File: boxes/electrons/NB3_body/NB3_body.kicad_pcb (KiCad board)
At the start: 2 copper layers, 200 x 199.5 mm, 45 parts, among them J1 Conn_02x05_Counter_Clockwise, J10 JST SH 4-way Socket, J12 Conn_02x03_Top_Bottom, J13 Conn_02x03_Top_Bottom, J14 Conn_02x05_Counter_Clockwise, J15 Conn_02x05_Counter_Clockwise, J2 Conn_02x05_Counter_Clockwise, J3 Conn_02x05_Counter_Clockwise, J4 Conn_02x05_Counter_Clockwise, J5 Conn_02x05_Counter_Clockwise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

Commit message: Work on PCBs (v1 and v2)
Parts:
- added H31: MountingHole, MountingHole:MountingHole_2.7mm_M2.5_ISO7380_Pad, F.Cu at (94.0, 161.0)
- added H32: MountingHole, MountingHole:MountingHole_2.7mm_M2.5_ISO7380_Pad, F.Cu at (155.0, 161.0)
- added J11: JST SH 4-way Socket, NB3_body:Connector_S4B-PH-SM4-TB(LF)(SN), F.Cu at (124.5, 78.0)
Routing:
- net /WS: track 320.0 -> 163.1 mm, vias 10 -> 6
- net /SDI: track 251.1 -> 99.5 mm, vias 6 -> 3
- net +3V3: track 271.5 -> 132.1 mm, vias 8 -> 5
- net /SCK: track 290.6 -> 157.4 mm, vias 4 -> 3
- net /LE: track 246.1 -> 172.1 mm
- net /LF: track 240.9 -> 170.1 mm
- net /LG: track 235.7 -> 168.2 mm
- net /LD: track 226.0 -> 159.0 mm
- net /LH: track 230.6 -> 166.4 mm
- net GND: track 128.0 -> 136.8 mm, vias 36 -> 42
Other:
- outline, holes or cut-outs redrawn
- board text added: "NB3_body Rev 0.0.6 For Research and Education ONLY"
- board text removed: "NB3_body Rev 0.0.5 For Research and Education ONLY"

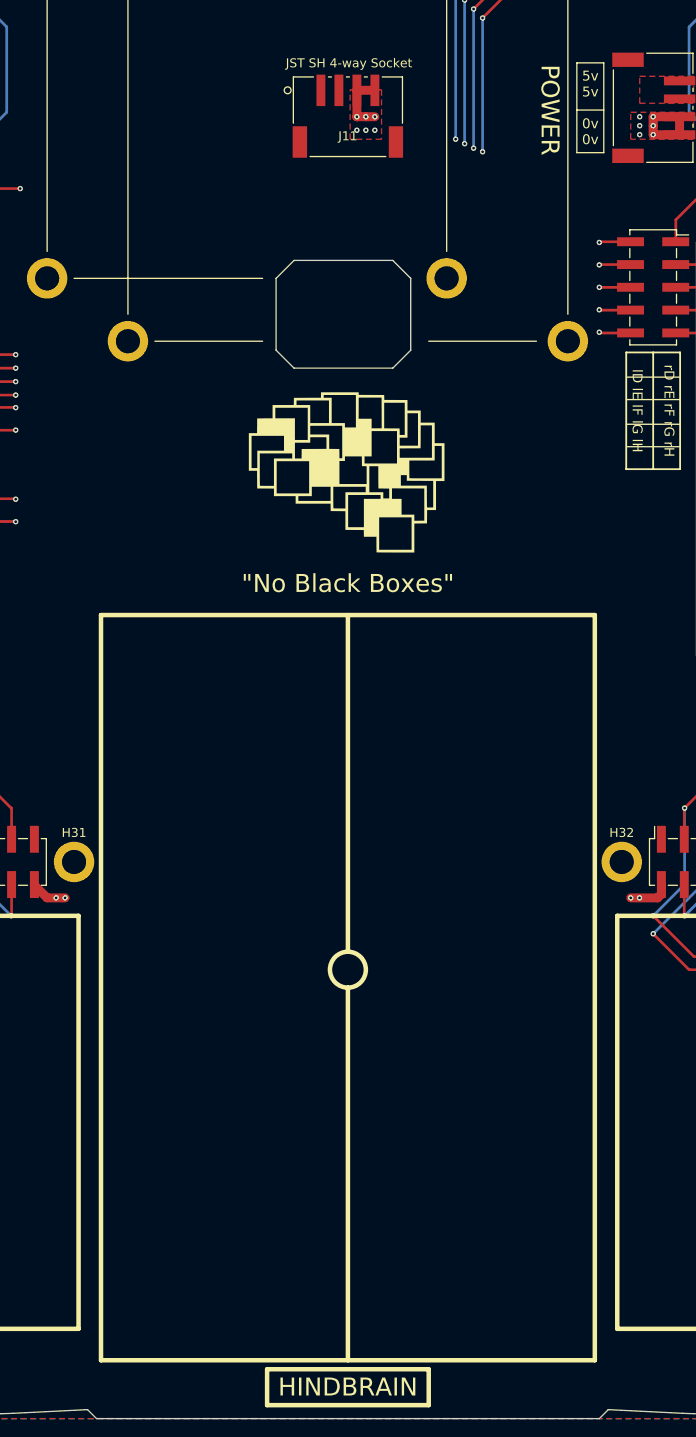
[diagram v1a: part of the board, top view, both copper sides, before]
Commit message: PCB tweaks (charger and body)
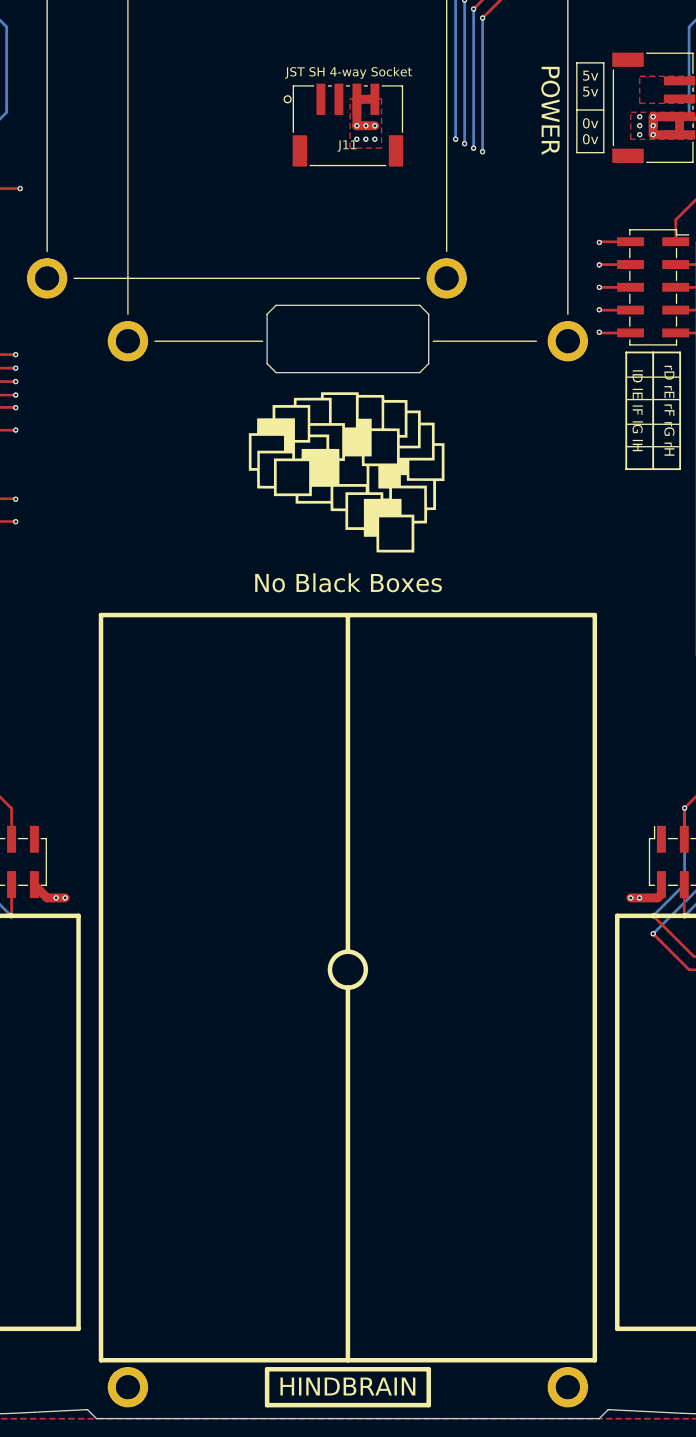
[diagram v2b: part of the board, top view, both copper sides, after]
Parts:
- moved H31 58.8 mm to (100.0, 219.5)
- moved H32 58.8 mm to (149.0, 219.5)
- moved J11 1.00 mm to (124.5, 79.0)
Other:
- outline, holes or cut-outs redrawn
- board text added: "No Black Boxes"
- board text removed: "{dblquote}No Black Boxes{dblquote}"

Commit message: Update NB3 Body (rev 6)
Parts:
- added G***: LOGO, NB3_body:Logo_VK_15mm, B.Cu at (124.5, 196.0)
- J12, J13: footprint Connector_PinHeader_2.54mm:PinHeader_2x03_P2.54mm_Vertical_SMD -> Connector_PinHeader_2.54mm:PinHeader_2x03_P2.54mm_Vertical
- moved J13 2.85 mm to (200.2, 166.5)
- moved J12 2.83 mm to (46.2, 166.5)
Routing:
- net /SCK: track 157.4 -> 326.8 mm, vias 3 -> 7
- net /WS: track 163.1 -> 323.8 mm, vias 6 -> 8
- net /SDI: track 99.5 -> 259.9 mm, vias 3 -> 7
- net +3V3: track 132.1 -> 285.2 mm, vias 5 -> 7
- net /LG: track 168.2 -> 249.9 mm
- net /LF: track 170.1 -> 251.5 mm
- net /LE: track 172.1 -> 252.8 mm
- net /LH: track 166.4 -> 245.1 mm
- net /LD: track 159.0 -> 237.6 mm
- net /LB: track 183.9 -> 188.1 mm
- net /LA: track 190.6 -> 189.2 mm
- net /RA: track 201.3 -> 202.5 mm

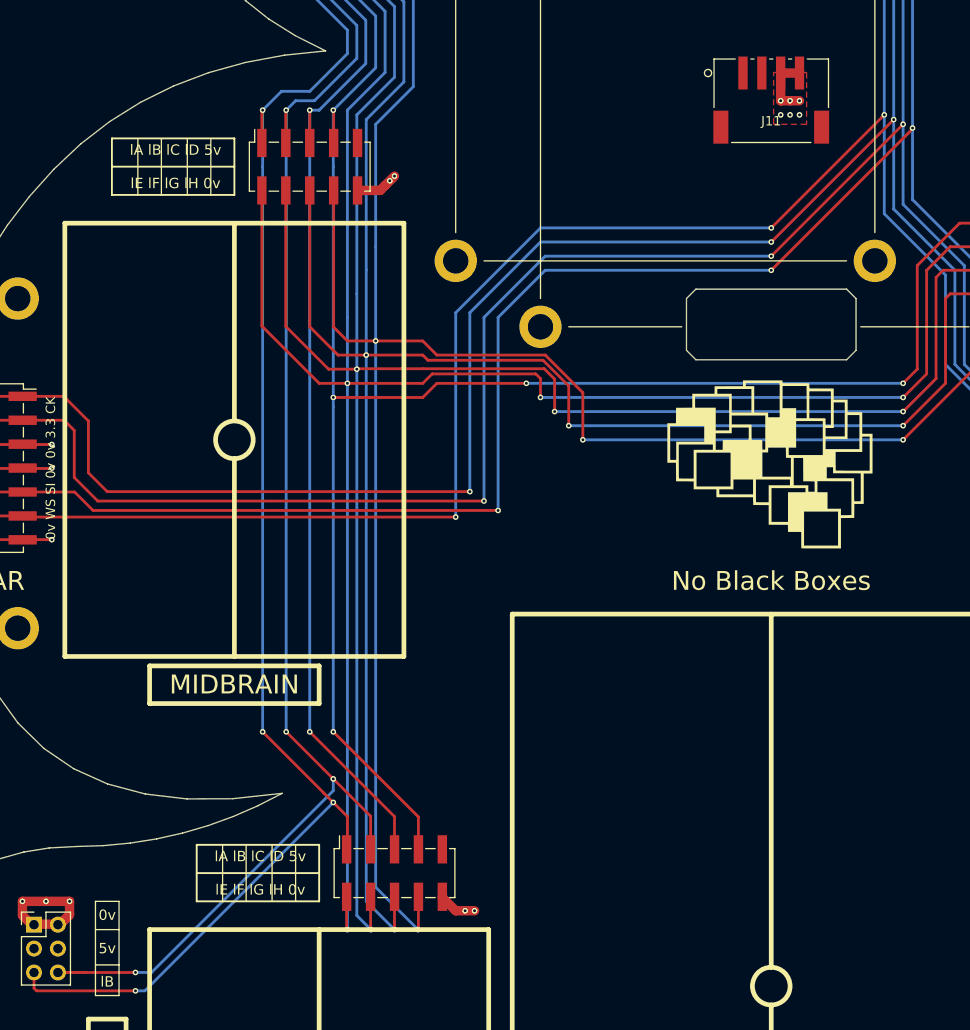
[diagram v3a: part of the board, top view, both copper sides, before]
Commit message: Update NB3 body wiring
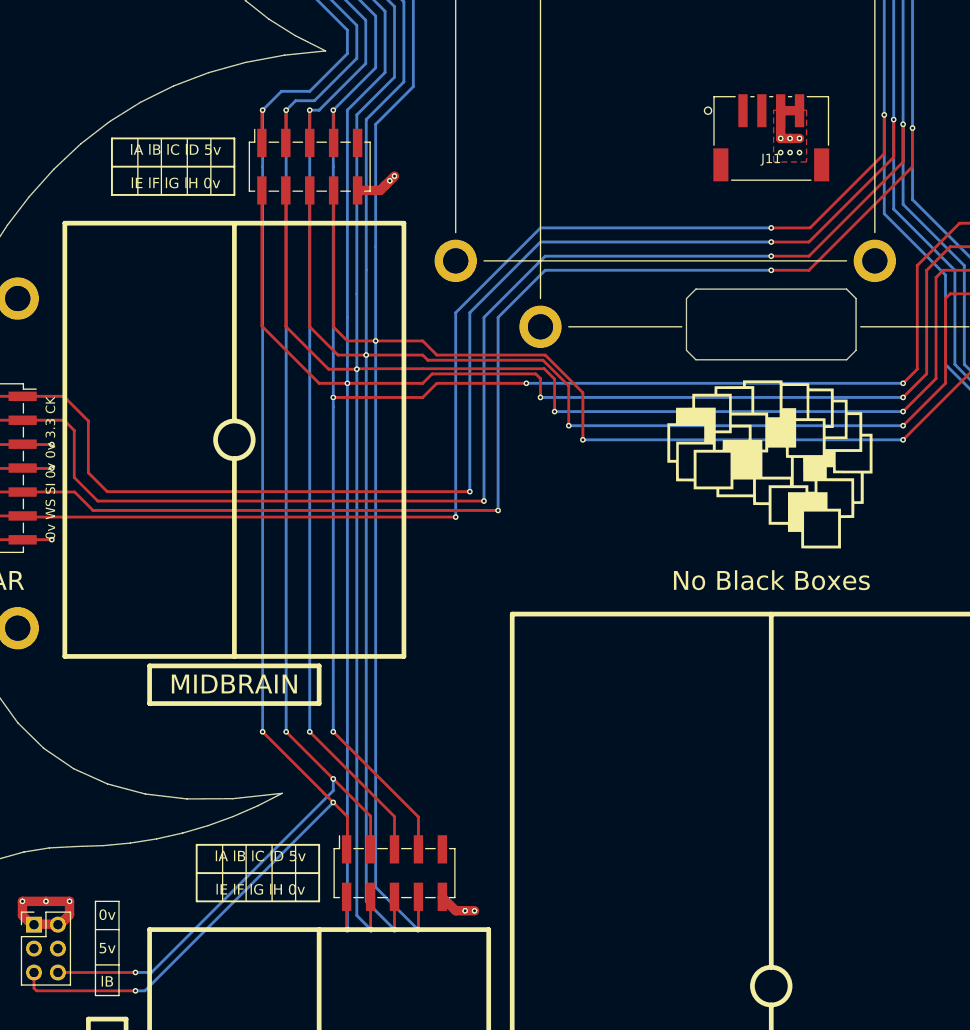
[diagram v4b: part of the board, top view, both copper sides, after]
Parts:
- moved J11 4.00 mm to (124.5, 83.0)
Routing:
- net /LB: track 188.1 -> 185.1 mm
- net /WS: track 323.8 -> 326.2 mm
- net /SDI: track 259.9 -> 262.3 mm
- net +3V3: track 285.2 -> 287.5 mm
- net /SCK: track 326.8 -> 329.1 mm
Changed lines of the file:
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@@
 		(grid_origin 124.5 223)
 		(pcbplotparams
-			(layerselection 0x00010fc_ffffffff)
+			(layerselection 0x0001000_7ffffffe)
 			(plot_on_all_layers_selection 0x0000000_00000000)
 			(disableapertmacros no)
@@
 			(sketchpadsonfab no)
 			(subtractmaskfromsilk no)
-			(outputformat 1)
+			(outputformat 3)
 			(mirror no)
 			(drillshape 0)
@@
 		(locked yes)
 		(layer "F.Cu")
-		(at 124.5 79 180)
+		(at 124.5 83 180)
 		(property "Reference" "J11"
 			(at 0.000001 -2.159 0)
@@
 	)
 	(segment
-		(start 51.7 171.55)
-		(end 51.695 171.555)
-		(width 0.3)
-		(layer "F.Cu")
-		(net 3)
-	)
-	(segment
 		(start 81.96 35.48)
 		(end 81.96 32.04)
@@
 	)
 	(segment
-		(start 51.695 171.555)
-		(end 48.765 171.555)
-		(width 0.3)
-		(layer "F.Cu")
-		(net 3)
-	)
-	(segment
 		(start 77 150)
 		(end 81.96 154.96)
@@
 	)
 	(segment
-		(start 125.499999 78.999999)
-		(end 125.5 79)
+		(start 125.499999 82.999999)
+		(end 125.5 83)
 		(width 1)
 		(locked yes)
@@
 	)
 	(segment
-		(start 125.5 79)
-		(end 126.5 79)
+		(start 125.5 83)
+		(end 126.5 83)
 		(width 1)
 		(locked yes)
@@
 	)
 	(segment
-		(start 126.5 79)
-		(end 127.5 79)
+		(start 126.5 83)
+		(end 127.5 83)
 		(width 1)
 		(locked yes)
@@
 	)
 	(segment
-		(start 125.499999 76.055299)
-		(end 127.499998 76.055299)
+		(start 125.499999 80.055299)
+		(end 127.499998 80.055299)
 		(width 1)
 		(locked yes)
@@
 	)
 	(segment
-		(start 125.499999 76.055299)
-		(end 125.499999 78.999999)
+		(start 125.499999 80.055299)
+		(end 125.499999 82.999999)
 		(width 1)
 		(locked yes)
@@
 	)
 	(via
-		(at 126.5 79)
+		(at 126.5 83)
 		(size 0.6)
 		(drill 0.3)
@@
 	)
 	(via
-		(at 127.5 80.5)
+		(at 127.5 84.5)
 		(size 0.6)
 		(drill 0.3)
@@
 	)
 	(via
-		(at 125.5 79)
+		(at 125.5 83)
 		(size 0.6)
 		(drill 0.3)
@@
 	)
 	(via
-		(at 126.5 80.5)
+		(at 126.5 84.5)
 		(size 0.6)
 		(drill 0.3)
@@
 	)
 	(via
-		(at 127.5 79)
+		(at 127.5 83)
 		(size 0.6)
 		(drill 0.3)
@@
 	)
 	(via
-		(at 125.5 80.5)
+		(at 125.5 84.5)
 		(size 0.6)
 		(drill 0.3)
@@
 	)
 	(segment
-		(start 137.5 81)
-		(end 124.5 94)
-		(width 0.3)
-		(layer "F.Cu")
-		(net 19)
-	)
-	(segment
 		(start 120.5 46)
 		(end 126.5 52)
@@
 	)
 	(segment
+		(start 128.5 94)
+		(end 124.5 94)
+		(width 0.3)
+		(layer "F.Cu")
+		(net 19)
+	)
+	(segment
 		(start 145.5 57)
 		(end 137.5 65)
@@
 	)
 	(segment
+		(start 137.5 81)
+		(end 137.5 85)
+		(width 0.3)
+		(layer "F.Cu")
+		(net 19)
+	)
+	(segment
 		(start 140.5 52)
 		(end 145.5 57)
@@
 	)
 	(segment
+		(start 137.5 85)
+		(end 128.5 94)
+		(width 0.3)
+		(layer "F.Cu")
+		(net 19)
+	)
+	(segment
 		(start 52 113)
 		(end 49.38 110.38)
@@
 	)
 	(segment
-		(start 138.5 81.5)
-		(end 124.5 95.5)
-		(width 0.3)
-		(layer "F.Cu")
-		(net 20)
-	)
-	(segment
 		(start 198.6 110.4)
 		(end 200.9 110.4)
@@
 	)
 	(segment
+		(start 128.5 95.5)
+		(end 124.5 95.5)
+		(width 0.3)
+		(layer "F.Cu")
+		(net 20)
+	)
+	(segment
 		(start 200.92 123.08)
 		(end 203.98 123.08)
@@
 	)
 	(segment
+		(start 138.5 81.5)
+		(end 138.5 85.5)
+		(width 0.3)
+		(layer "F.Cu")
+		(net 20)
+	)
+	(segment
 		(start 203.98 110.38)
 		(end 209.02 110.38)
@@
 		(net 20)
 	)
+	(segment
+		(start 138.5 85.5)
+		(end 128.5 95.5)
+		(width 0.3)
+		(layer "F.Cu")
+		(net 20)
+	)
 	(via
 		(at 164 111.5)
@@
 	)
 	(segment
+		(start 128.5 97)
+		(end 124.5 97)
+		(width 0.3)
+		(layer "F.Cu")
+		(net 21)
+	)
+	(segment
 		(start 52.5 122.5)
 		(end 50.54 120.54)
@@
 	)
 	(segment
-		(start 139.5 82)
-		(end 124.5 97)
+		(start 139.5 81.9)
+		(end 139.5 86)
 		(width 0.3)
 		(layer "F.Cu")
@@
 	)
 	(segment
-		(start 39.98 120.54)
-		(end 45.02 120.54)
+		(start 139.5 86)
+		(end 128.5 97)
 		(width 0.3)
 		(layer "F.Cu")
@@
 	)
 	(segment
-		(start 139.5 81.9)
-		(end 139.5 82)
+		(start 39.98 120.54)
+		(end 45.02 120.54)
 		(width 0.3)
 		(layer "F.Cu")
@@
 	)
 	(segment
+		(start 136.5 84.625)
+		(end 128.625 92.5)
+		(width 0.3)
+		(layer "F.Cu")
+		(net 22)
+	)
+	(segment
 		(start 121.96 36.54)
 		(end 121.96 33.52)
@@
 	)
 	(segment
-		(start 197.5 113.5)
-		(end 198.08 112.92)
+		(start 128.625 92.5)
+		(end 124.5 92.5)
 		(width 0.3)
 		(layer "F.Cu")
@@
 	)
 	(segment
-		(start 136.5 80.5)
-		(end 124.5 92.5)
+		(start 197.5 113.5)
+		(end 198.08 112.92)
 		(width 0.3)
 		(layer "F.Cu")
@@
 		(net 22)
 	)
+	(segment
+		(start 136.5 80.5)
+		(end 136.5 84.625)
+		(width 0.3)
+		(layer "F.Cu")
+		(net 22)
+	)
 	(via
 		(at 164.5 57)
@@
 		(polygon
 			(pts
-				(xy 124.75 76) (xy 128.25 76) (xy 128.25 81.5) (xy 124.75 81.5)
+				(xy 124.75 80) (xy 128.25 80) (xy 128.25 85.5) (xy 124.75 85.5)
 			)
 		)

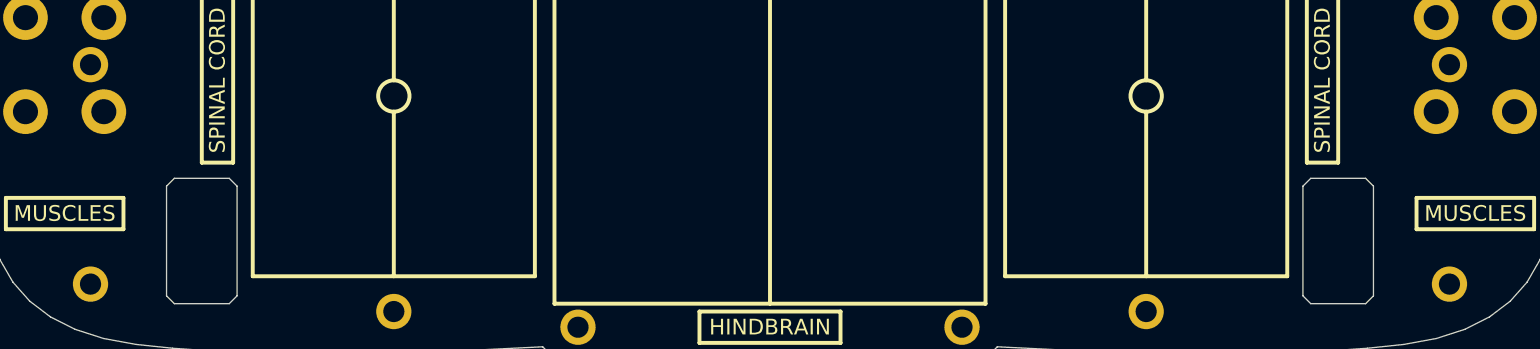
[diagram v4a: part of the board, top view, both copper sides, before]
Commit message: Update NB3 Body (servo mounts for metal motors)
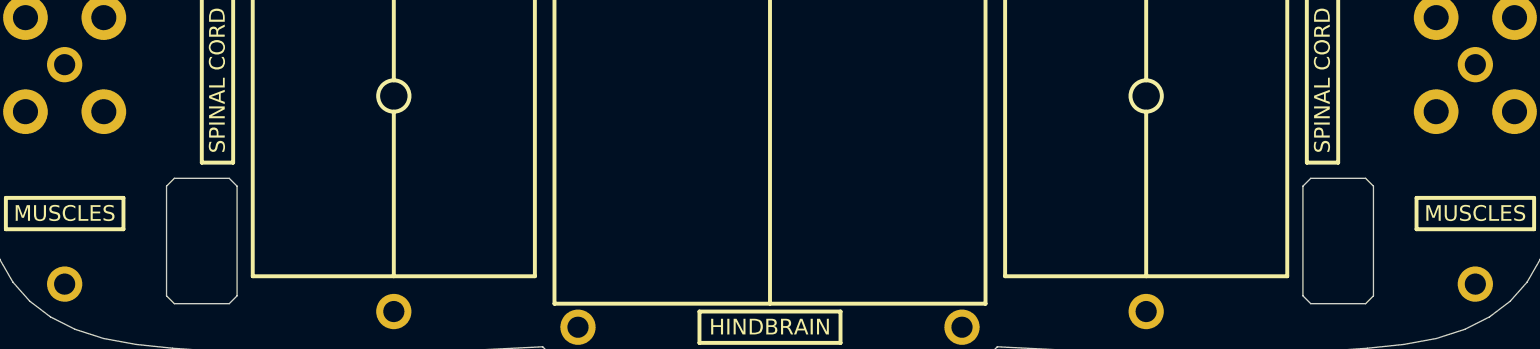
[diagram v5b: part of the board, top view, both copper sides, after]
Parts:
- moved H24 3.30 mm to (214.5, 186.0)
- moved H26 3.30 mm to (214.5, 214.0)
- moved H23 3.30 mm to (34.5, 186.0)
- moved H25 3.30 mm to (34.5, 214.0)
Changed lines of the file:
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@@
 		(locked yes)
 		(layer "F.Cu")
-		(at 37.8 186)
+		(at 34.5 186)
 		(descr "Mounting Hole 2.7mm, M2.5, ISO7380")
 		(tags "mounting hole 2.7mm m2.5 iso7380")
@@
 		(locked yes)
 		(layer "F.Cu")
-		(at 211.2 214)
+		(at 214.5 214)
 		(descr "Mounting Hole 2.7mm, M2.5, ISO7380")
 		(tags "mounting hole 2.7mm m2.5 iso7380")
@@
 		(locked yes)
 		(layer "F.Cu")
-		(at 37.8 214)
+		(at 34.5 214)
 		(descr "Mounting Hole 2.7mm, M2.5, ISO7380")
 		(tags "mounting hole 2.7mm m2.5 iso7380")
@@
 		(locked yes)
 		(layer "F.Cu")
-		(at 211.2 186)
+		(at 214.5 186)
 		(descr "Mounting Hole 2.7mm, M2.5, ISO7380")
 		(tags "mounting hole 2.7mm m2.5 iso7380")

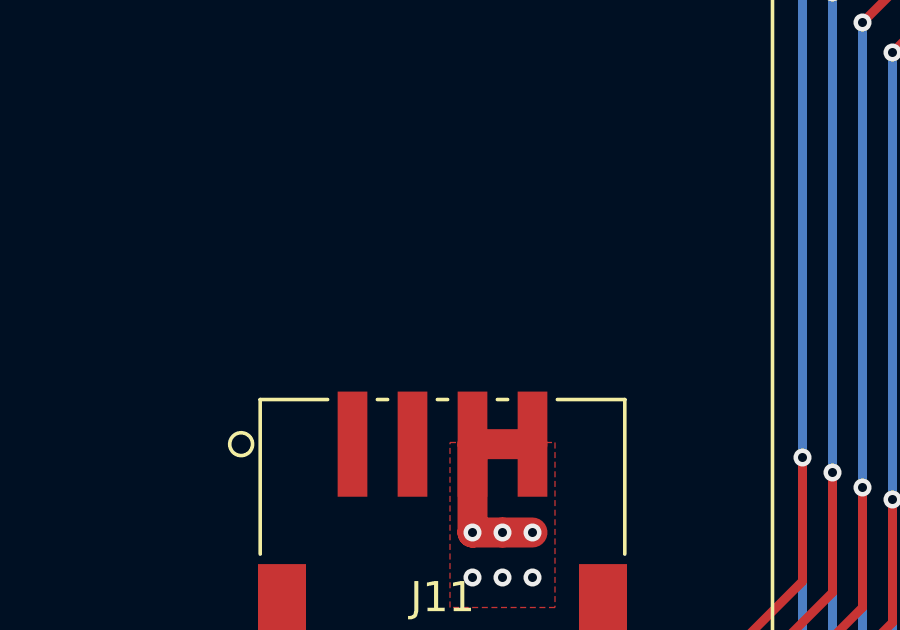
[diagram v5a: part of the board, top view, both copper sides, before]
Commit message: Work on NB3 charger PCB layout
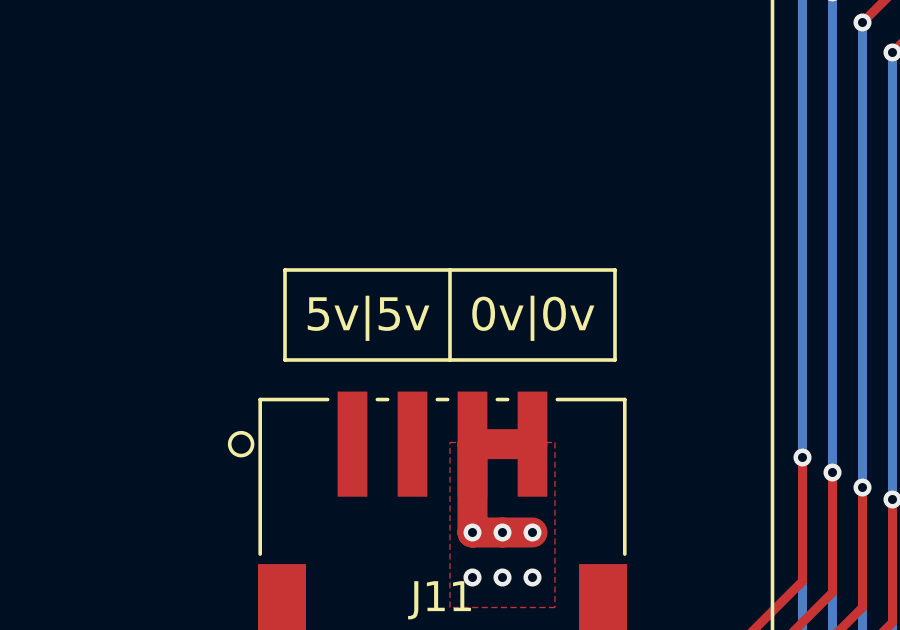
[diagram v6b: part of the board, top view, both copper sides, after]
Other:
- board text added: "0v|0v"
- board text added: "5v|5v"
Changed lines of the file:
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@@
 		(layer "F.SilkS")
 	)
+	(gr_rect
+		(start 119.25 74.25)
+		(end 130.25 77.25)
+		(stroke
+			(width 0.12)
+			(type solid)
+		)
+		(fill none)
+		(layer "F.SilkS")
+	)
 	(gr_line
 		(start 181.5 83.25)
@@
 	)
 	(gr_line
+		(start 124.75 77.25)
+		(end 124.75 74.25)
+		(stroke
+			(width 0.12)
+			(type solid)
+		)
+		(layer "F.SilkS")
+	)
+	(gr_line
 		(start 133.5 221.5)
 		(end 115.5 221.5)
@@
 		)
 	)
+	(gr_text "0v|0v"
+		(at 127.5 75.75 0)
+		(layer "F.SilkS")
+		(effects
+			(font
+				(size 1.1 1.1)
+				(thickness 0.25)
+			)
+		)
+	)
 	(gr_text "lA lB lC lD 5v\n\nlE lF lG lH 0v"
 		(at 99 38 0)
@@
 		(layer "F.SilkS")
 		(effects
+			(font
+				(size 1.1 1.1)
+				(thickness 0.25)
+			)
+		)
+	)
+	(gr_text "5v|5v"
+		(at 122 75.75 0)
+		(layer "F.SilkS")
+		(effects
